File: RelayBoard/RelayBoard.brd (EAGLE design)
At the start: 139.1 x 115.2 mm, 97 parts, among them IC1 MCP2551/SN RSC 402-904, J4 JTAG_ARM_10PIN, U1 CD74HC4067SM96, U2 LM1084IS-3.3, U3 CD74HC4067SM96, U4 CD74HC4067SM96, U5 CD74HC4067SM96, U6 LM1084IS-3.3, U7 LM1084IS-3.3, U8 TM4C1294NCPDT, X1 A1944-50, X2 A1944-50, X3 A1944-50, X4 A1944-50, Y3 NX3225GA, Y4 CRYATL_32K_SMD

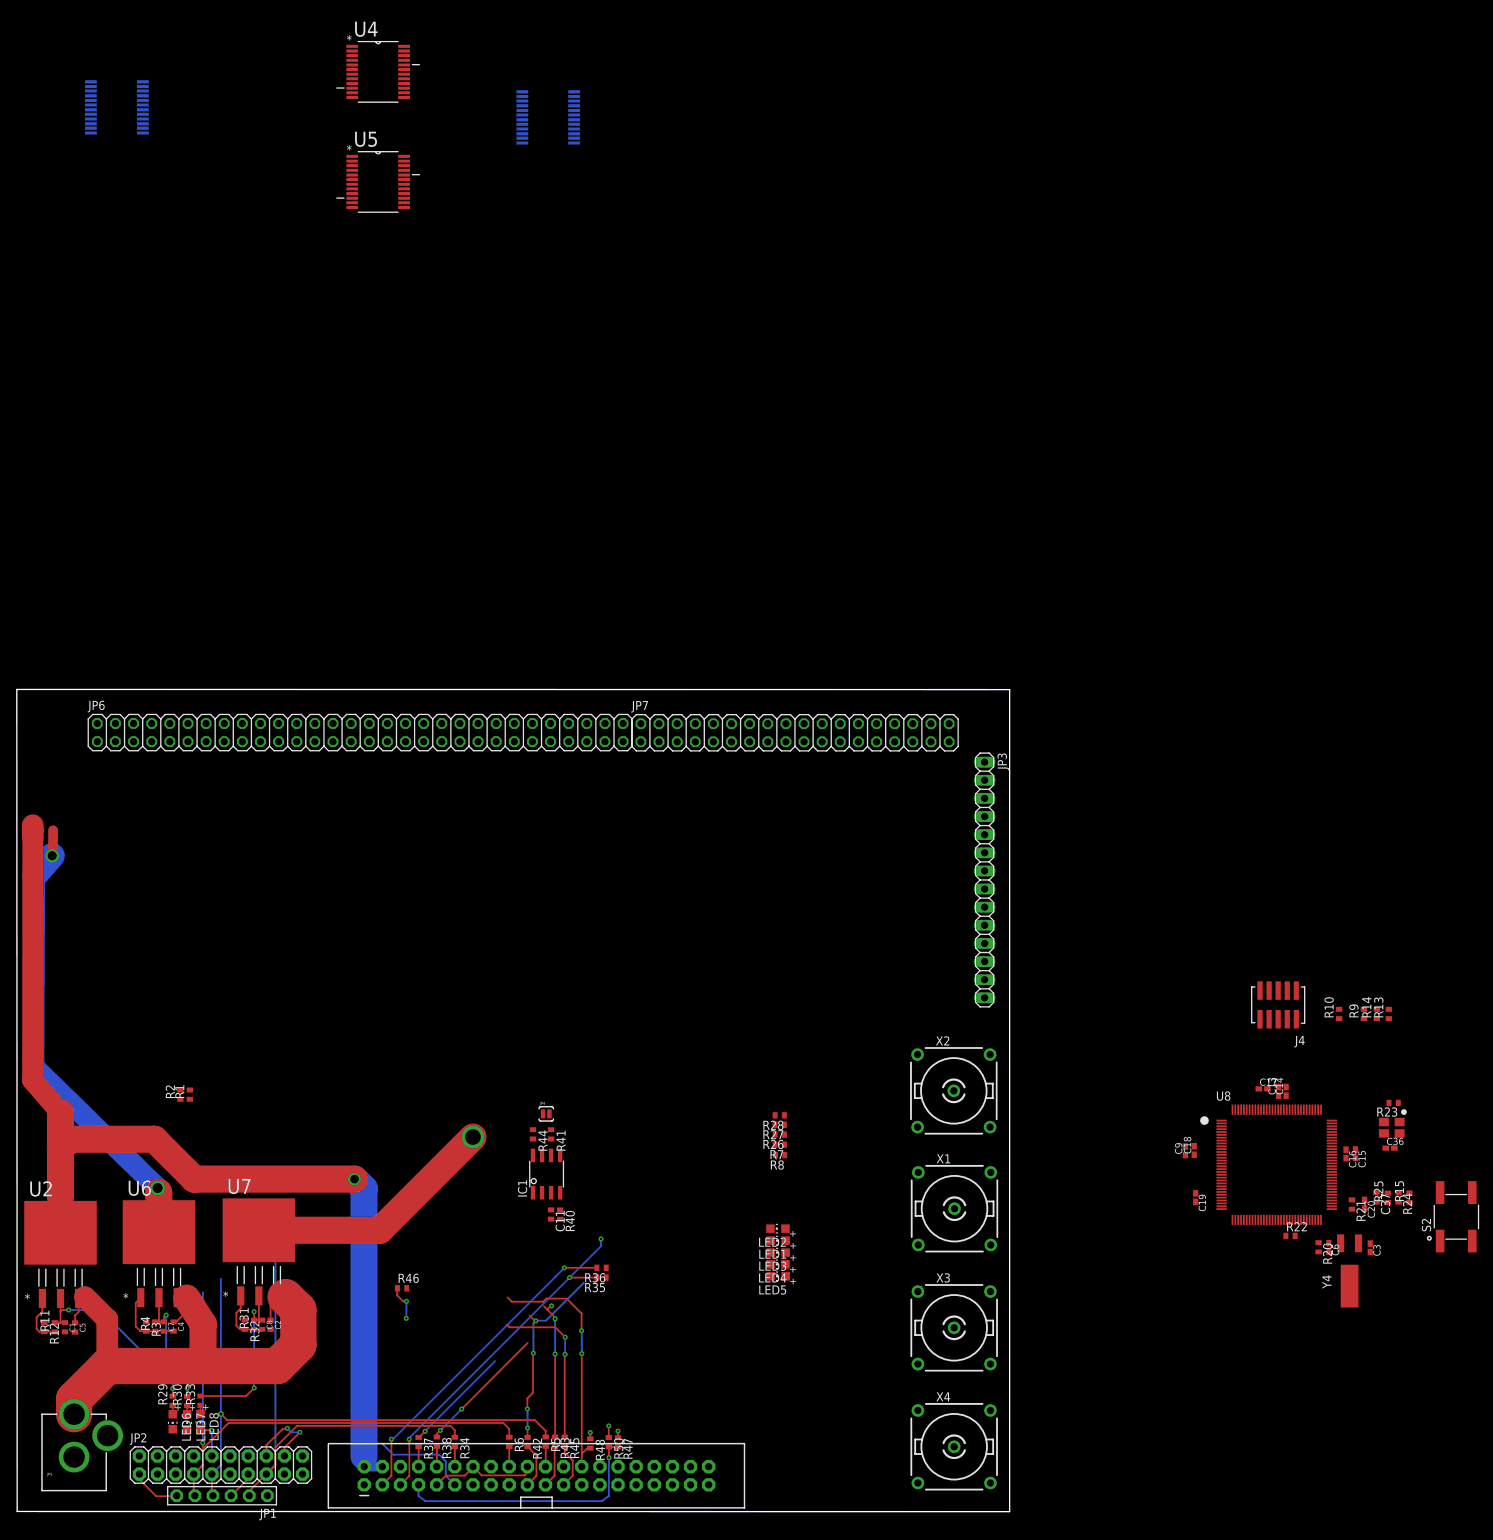
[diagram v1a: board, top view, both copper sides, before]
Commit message: additions
- common connector for isp, jtag, swd
- change LDOs to the one which have Enable pin
- UART -> USB interface and isolator to the uart side
- dedicated MCU supply
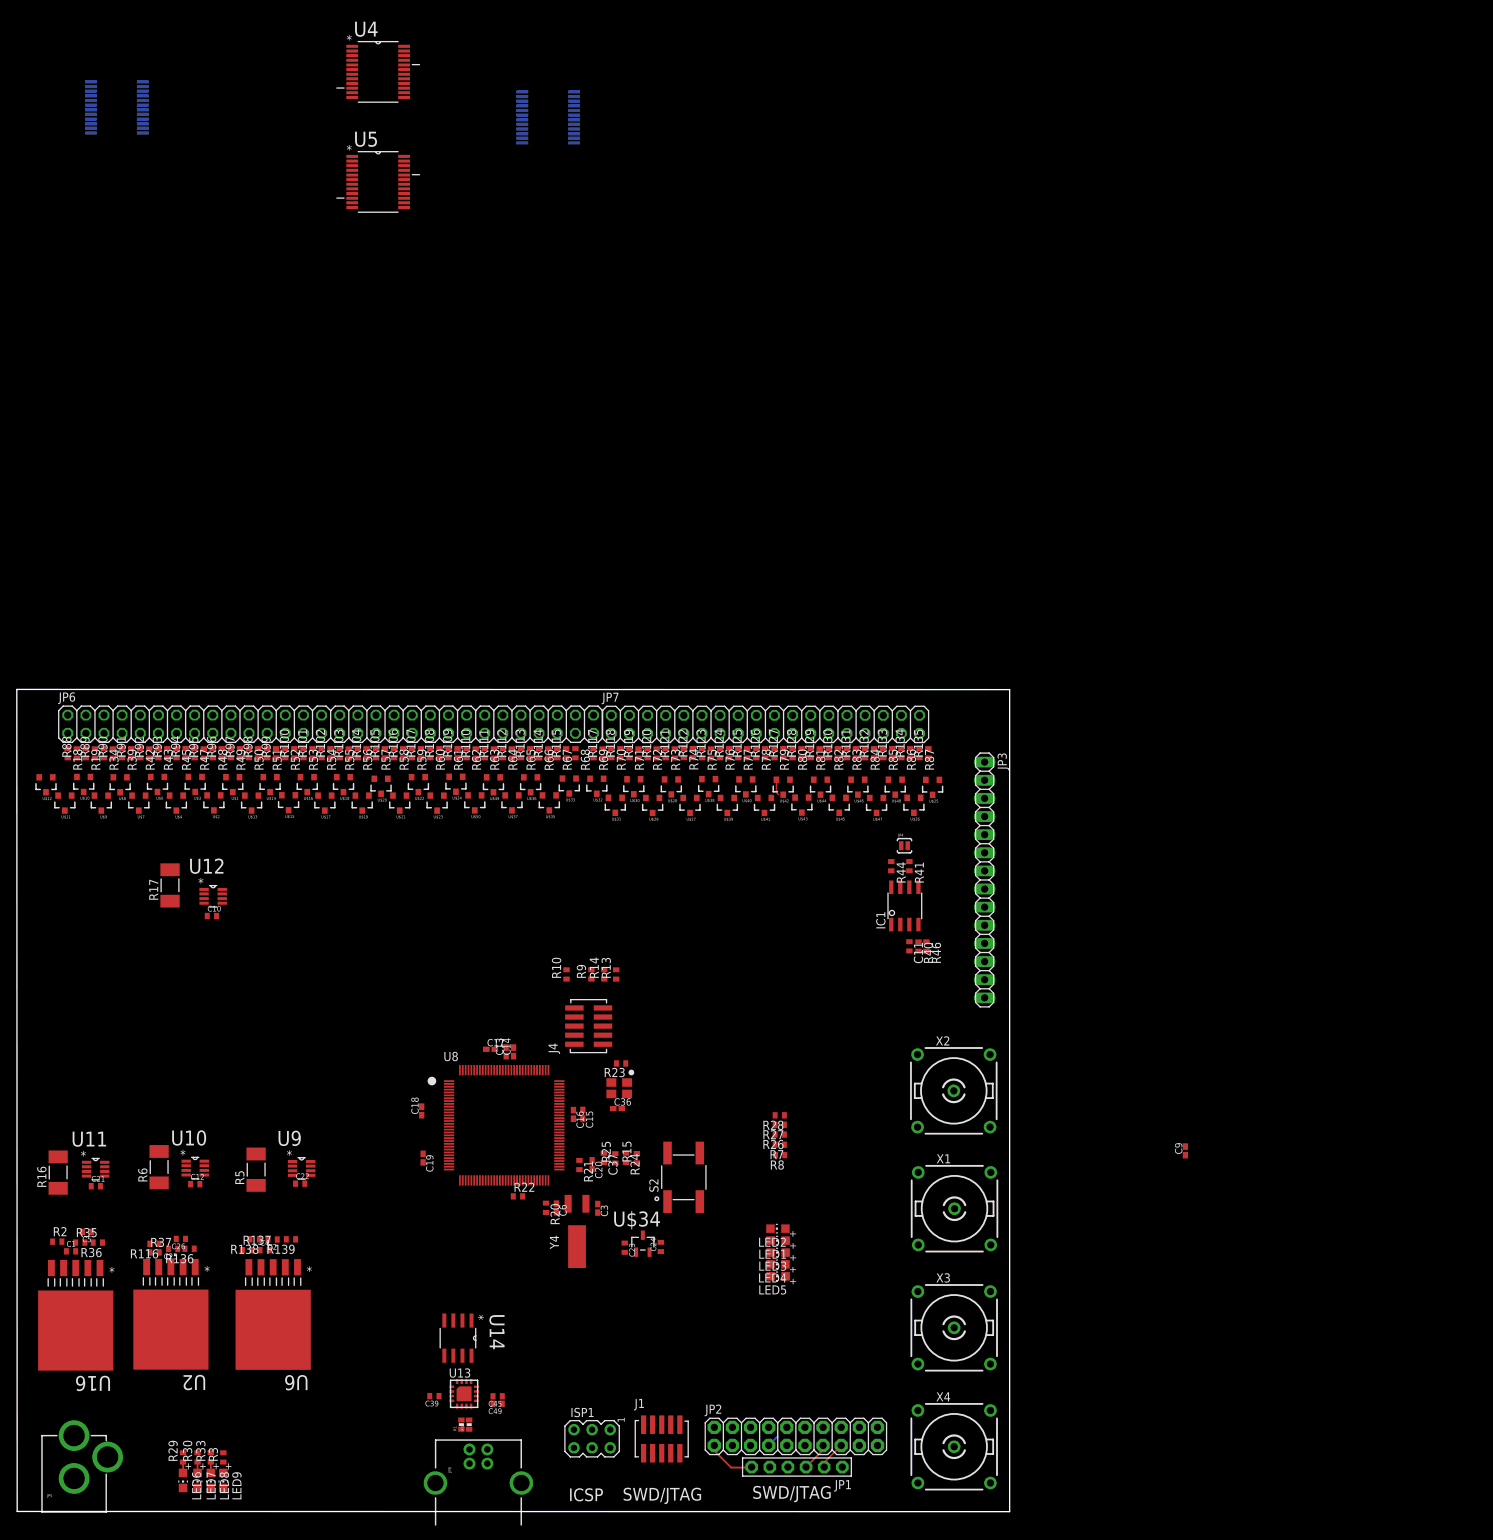
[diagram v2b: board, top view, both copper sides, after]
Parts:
- removed C7, C8: 10uF, rcl:C0402
- removed JP30: RASPBERRYPI-B+-GPIO, SparkFun-Boards:2X20-SHROUDED
- removed R11, R12, R31, R32, R4: (no value), resistor:R0402@1
- removed U7: LM1084IS-3.3, LDO:TO254P1435X457-3N
- added C10, C12, C21, C22, C39, C45: 0.1uF, rcl:C0402
- added C23, C24: 1uF, rcl:C0402
- added C25, C26, C49: 10uF, rcl:C0402
- added ISP1: AVRISP-6, JDT-1800_smahed:AVRISP
- added J1: JTAG_ARM_10PIN, MRDT-Connectors:CON_2X5_50MIL
- added JP8: USB-B, SparkFun-Connectors:USB-B-PTH
- added LED9: (no value), JDT-1800_smahed:CHIP-LED0805
- added R100, R101, R102, R103, R104, R105, R106, R107, R108, R109, R110, R111, R112, R113, R114, R115, R117, R118, R119, R120, R121, R122, R123, R124, R125, R126, R127, R128, R129, R130, R131, R132, R133, R134, R135, R18, R19, R39, R49, R51, R52, R53, R54, R55, R56, R57, R58, R59, R60, R61, R62, R63, R64, R65, R66, R67, R68, R69, R70, R71, R72, R73, R74, R75, R76, R77, R78, R79, R80, R81, R82, R83, R84, R85, R86, R87, R88, R89, R90, R91, R92, R93, R94, R95, R96, R97, R98, R99: 200R, resistor:R0402
- added R116, R136, R137, R138, R139: (no value), resistor:R0402
- added R16, R17: (no value), JDT-1800_smahed:R5025
- added U$1, U$10, U$11, U$12, U$13, U$14, U$15, U$16, U$17, U$18, U$19, U$2, U$20, U$21, U$22, U$23, U$24, U$25, U$26, U$27, U$28, U$29, U$3, U$30, U$31, U$32, U$33, U$35, U$36, U$37, U$38, U$39, U$4, U$40, U$41, U$42, U$43, U$44, U$45, U$46, U$47, U$48, U$49, U$50, U$6, U$7, U$8, U$9: zener_3.3V, SparkFun-DiscreteSemi:SOT23-3
- added U$34: MCP1703T-3302E/CB, MCP1703:SOT95P300X145-3N
- added U10, U11, U12, U9: INA219AIDCNR, INA219:SOT65P280X145-8N
- added U13: FT230XQ, ftdichip:QFN16
- added U14: ADUM1201ARZ, ADUM1201ARZ:SOIC127P600X175-8N
- added U16: TL1963AKTTR., TL1963:TO170P1485X457-6N
- C2, C4, C5: value 0.1uF -> 10uF
- R1, R38: value (none) -> 22R; device resistor:R0402@1 -> SparkFun-Passives:0402-RES
- R10, R13, R14, R15, R2, R26, R27, R28, R29, R3, R30, R33, R35, R36, R37, R40, R41, R44, R46, R7, R8, R9: device resistor:R0402@1 -> resistor:R0402
- R34, R42, R43, R45, R50: value 0R -> 200R; device resistor:R0402@1 -> resistor:R0402
- R47, R48: value 10k -> 200R; device resistor:R0402@1 -> resistor:R0402
- R5, R6: value 0R -> (none); device resistor:R0402@1 -> JDT-1800_smahed:R5025
- U2, U6: value LM1084IS-3.3 -> TL1963AKTTR.; device LDO:TO254P1435X457-3N -> TL1963:TO170P1485X457-6N
- moved R47 113.3 mm to (25.2, 106.1)
- moved R43 111.3 mm to (20.1, 106.1)
- moved R45 110.7 mm to (22.7, 106.1)
- moved R42 110.7 mm to (17.6, 106.1)
- moved R48 110.2 mm to (27.8, 106.1)
- moved R50 108.9 mm to (32.8, 106.1)
- moved C16 108.4 mm to (78.3, 55.5)
- moved C17 108.4 mm to (66.7, 64.6)
- moved C36 108.4 mm to (84.5, 56.3)
- moved C37 108.4 mm to (82.5, 49.4)
- moved R21 108.4 mm to (79.1, 48.4)
- moved R25 108.4 mm to (84.2, 49.4)
- moved R9 108.4 mm to (80.8, 75.1)
- moved C13 108.4 mm to (68.9, 64.3)
- moved C14 108.4 mm to (69.9, 64.3)
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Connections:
- removed net +3V3: C16.1, C17.1, C18.1, C19.1, J4.P1, R20.2, R21.2, R25.1, U8.P$101, U8.P$113, U8.P$122, U8.P$16, U8.P$26, U8.P$28, U8.P$39, U8.P$47, U8.P$51, U8.P$52, U8.P$69, U8.P$7, U8.P$79, U8.P$8, U8.P$9, U8.P$90
- removed net 3.3V: JP30.17
- removed net 3.6V: C8.1, R31.2, R33.2, U7.2, U7.4
- removed net 5V: C1.1, JP30.2, JP30.4, R11.2, R29.2, U2.2, U2.4
- removed net A0: U3.17, U5.17
- removed net A1: U3.16, U5.16
- removed net A2: U3.19, U5.19
- removed net A3: U3.18, U5.18
- removed net ADJ: R3.2, R4.1, U6.1
- removed net ADJ1: R11.1, R12.2, U2.1
- removed net ADJ2: R31.1, R32.2, U7.1
- removed net CAN_CS: JP30.26, R48.2
- removed net D0: U3.21, U5.21
- removed net D1: U3.20, U5.20
- removed net D10: U3.9, U5.9
- removed net D11: U3.8, U5.8
- removed net D12: U1.17, U4.17
- removed net D13: U1.16, U4.16
- removed net D14: U1.19, U4.19
- removed net D15: U1.18, U4.18
- removed net D16: U1.21, U4.21
- removed net D17: U1.20, U4.20
- removed net D18: U1.23, U4.23
- removed net D19: U1.22, U4.22
- removed net D2: U3.23, U5.23
- removed net D20: U1.8, U4.8
- removed net D21: U1.9, U4.9
- removed net D22: U1.6, U4.6
- removed net D23: U1.7, U4.7
- removed net D24: U1.4, U4.4
- removed net D25: U1.5, U4.5
- removed net D26: U1.2, U4.2
- removed net D27: U1.3, U4.3
- removed net D3: U3.22, U5.22
- removed net D4: U3.4, U5.4
- removed net D5: U3.5, U5.5
- removed net D6: U3.2, U5.2
- removed net D7: U3.3, U5.3
- removed net D8: U3.7, U5.7
- removed net D9: U3.6, U5.6
- removed net IO_INT: JP30.11
- removed net NC0: JP30.1
- removed net RPI_NRESET: JP30.12, R34.2
- removed net RPI_SWDCLK: JP30.22, R5.2
- removed net RPI_SWDIO: JP30.18, R6.2
- removed net RX: J4.P7, JP3.10, R38.1, U8.P$33
- removed net SCK: R45.1
- removed net TARGET_CS: JP30.7, R47.2, R50.2
- removed net TFT_CS: JP30.24
- removed net TFT_MISO: JP30.21, R43.2
- removed net TFT_MOSI: JP30.19, R42.2
- removed net TFT_RX: JP30.8, R37.2
- removed net TFT_SCK: JP30.23, R45.2
- removed net TFT_SCL: JP30.5, R1.1, R35.2
- removed net TFT_SDA: JP30.3, R2.1, R36.2
- removed net TFT_TX: JP30.10, R38.2
- removed net TX: J4.P9, JP3.11, R37.1, U8.P$34
- removed net VOLTAGE_INPUT: C2.1, C4.1, C5.1, JP5.PWR, U2.3, U6.3, U7.3
- new net ADJ3: R2.1, R35.2, U16.5
- new net ADJ4: R116.2, R37.1, U2.5
- new net ADJ5: R137.1, R138.2, U6.5
- new net DUT_SH+: R17.2, U12.1
- new net DUT_SH_-: R17.1, U12.2
- new net HOST_GND: C39.1, C45.1, C49.1, U13.13, U13.3, U14.5
- new net HOST_UART_RX: U13.2, U14.6
- new net HOST_UART_TX: U13.15, U14.2
- new net LDO1: R108.1, R16.2, R29.2, R60.2, U$22.1, U$22.2, U11.2
- new net LDO1_ENABLE: R36.1, U16.1
- new net LDO1_SH+: C1.1, R16.1, R2.2, U11.1, U16.4
- new net LDO2: R109.1, R30.2, R6.2, R61.2, U$23.1, U$23.2, U10.2
- new net LDO2_ENABLE: R136.1, U2.1
- new net LDO2_SH+: C2.1, R37.2, R6.1, U10.1, U2.4
- new net LDO3: R110.1, R33.2, R5.2, R62.2, U$24.1, U$24.2, U9.2
- new net LDO3_ENABLE: R139.1, U6.1
- new net LDO3_SH+: C4.1, R137.2, R5.1, U6.4, U9.1
- new net M0S0: U4.10
- new net M0S1: U4.11
- new net M0S2: U4.14
- new net M0S3: U4.13
- new net M3S0: U5.10
- new net M3S1: U5.11
- new net M3S2: U5.14
- new net M3S3: U5.13
- new net N$10: JP6.11, R43.1
- new net N$100: JP6.38, R106.2
- new net N$101: JP6.40, R107.2
- new net N$102: JP6.42, R108.2
- new net N$103: JP6.44, R109.2
- new net N$104: JP6.46, R110.2
- new net N$105: JP6.48, R111.2
- new net N$106: JP6.50, R112.2
- new net N$107: JP6.52, R113.2
- new net N$108: JP6.54, R114.2
- new net N$109: JP6.56, R115.2
- new net N$11: JP6.13, R45.1
- new net N$110: LED9.A, R3.1
- new net N$111: JP6.60, R117.2
- new net N$112: R18.2, U$12.2
- new net N$113: R87.2, U$25.2
- new net N$114: R88.1, U$12.1
- new net N$115: R89.1, U$11.1
- new net N$116: R19.2, U$11.2
- new net N$117: R90.1, U$10.1
- new net N$118: R34.2, U$10.2
- new net N$119: R91.1, U$9.1
- new net N$12: JP6.15, R47.1
- new net N$120: R39.2, U$9.2
- new net N$121: R92.1, U$8.1
- new net N$122: R42.2, U$8.2
- new net N$123: R43.2, U$7.2
- new net N$124: R93.1, U$7.1
- new net N$125: R94.1, U$6.1
- new net N$126: R45.2, U$6.2
- new net N$127: R47.2, U$4.2
- new net N$128: R95.1, U$4.1
- new net N$129: R96.1, U$3.1
- new net N$13: JP6.17, R48.1
- new net N$130: R48.2, U$3.2
- new net N$131: R97.1, U$2.1
- new net N$132: R49.2, U$2.2
- new net N$133: R50.2, U$1.2
- new net N$134: R98.1, U$1.1
- new net N$135: R99.1, U$13.1
- new net N$136: R51.2, U$13.2
- new net N$137: R52.2, U$14.2
- new net N$138: R100.1, U$14.1
- new net N$139: R101.1, U$15.1
- new net N$14: JP6.19, R49.1
- new net N$140: R53.2, U$15.2
- new net N$141: R54.2, U$16.2
- new net N$142: R102.1, U$16.1
- new net N$143: R55.2, U$17.2
- new net N$144: R103.1, U$17.1
- new net N$145: R104.1, U$18.1
- new net N$146: R56.2, U$18.2
- new net N$147: R105.1, U$19.1
- new net N$148: R57.2, U$19.2
- new net N$149: R106.1, U$20.1
- new net N$15: JP6.21, R50.1
- new net N$150: R58.2, U$20.2
- new net N$151: R59.2, U$21.2
- new net N$152: R107.1, U$21.1
- new net N$157: R135.1, U$25.1
- new net N$159: C39.2, U13.8
- new net N$16: JP6.23, R51.1
- new net N$160: R134.1, U$26.1
- new net N$161: R86.2, U$26.2
- new net N$162: R85.2, U$48.2
- new net N$163: R133.1, U$48.1
- new net N$164: R84.2, U$47.2
- new net N$165: R83.2, U$46.2
- new net N$166: R82.2, U$45.2
- new net N$167: R81.2, U$44.2
- new net N$168: R80.2, U$43.2
- new net N$169: R79.2, U$42.2
- new net N$17: JP6.25, R52.1
- new net N$170: R78.2, U$41.2
- new net N$171: R77.2, U$40.2
- new net N$172: R76.2, U$39.2
- new net N$173: R75.2, U$38.2
- new net N$174: R73.2, U$28.2
- new net N$175: R72.2, U$29.2
- new net N$176: R71.2, U$30.2
- new net N$177: R70.2, U$31.2
- new net N$178: R69.2, U$32.2
- new net N$179: R68.2, U$33.1
- new net N$18: JP6.27, R53.1
- new net N$180: R67.2, U$35.2
- new net N$181: R66.2, U$36.2
- new net N$182: R129.1, U$44.1
- new net N$183: R132.1, U$47.1
- new net N$184: R131.1, U$46.1
- new net N$185: R130.1, U$45.1
- new net N$186: R74.2, U$27.2
- new net N$187: R128.1, U$43.1
- new net N$188: R127.1, U$42.1
- new net N$189: R65.2, U$37.2
- new net N$19: JP6.29, R54.1
- new net N$190: R64.2, U$49.2
- new net N$191: R63.2, U$50.2
- new net N$192: R126.1, U$41.1
- new net N$193: R125.1, U$40.1
- new net N$194: R124.1, U$39.1
- new net N$195: R123.1, U$38.1
- new net N$196: R122.1, U$27.1
- new net N$197: R121.1, U$28.1
- new net N$198: R120.1, U$29.1
- new net N$199: R119.1, U$30.1
- new net N$20: JP6.31, R55.1
- new net N$200: R118.1, U$31.1
- new net N$201: R117.1, U$32.1
- new net N$203: R115.1, U$33.2
- new net N$204: R114.1, U$36.1
- new net N$205: R113.1, U$37.1
- new net N$206: R112.1, U$49.1
- new net N$207: R111.1, U$50.1
- new net N$21: JP6.33, R56.1
- new net N$216: C23.1, U$34.3
- new net N$22: JP6.35, R57.1
- new net N$24: JP6.37, R58.1
- new net N$26: JP6.39, R59.1
- new net N$27: JP6.41, R60.1
- new net N$28: JP6.43, R61.1
- new net N$29: JP6.45, R62.1
- new net N$30: JP6.47, R63.1
- new net N$31: JP6.49, R64.1
- new net N$32: JP6.51, R65.1
- new net N$37: JP6.53, R66.1
- new net N$38: JP6.55, R67.1
- new net N$39: JP6.57, R68.1
- new net N$4: JP6.1, R18.1
- new net N$40: JP6.59, R69.1
- new net N$41: JP7.1, R70.1
- new net N$42: JP7.3, R71.1
- new net N$43: JP7.5, R72.1
- new net N$49: JP7.7, R73.1
- new net N$50: JP7.9, R74.1
- new net N$51: JP7.11, R75.1
- new net N$52: JP7.13, R76.1
- new net N$53: JP7.15, R77.1
- new net N$54: JP7.17, R78.1
- new net N$55: JP7.19, R79.1
- new net N$56: JP7.21, R80.1
- new net N$57: JP7.23, R81.1
- new net N$58: JP7.25, R82.1
- new net N$59: JP7.27, R83.1
- new net N$6: JP6.3, R19.1
- new net N$60: JP7.29, R84.1
- new net N$61: JP7.31, R85.1
- new net N$62: JP7.33, R86.1
- new net N$63: JP7.35, R87.1
- new net N$64: JP7.2, R118.2
- new net N$65: JP7.4, R119.2
- new net N$66: JP7.6, R120.2
- new net N$67: JP7.8, R121.2
- new net N$68: JP7.10, R122.2
- new net N$69: JP7.12, R123.2
- new net N$7: JP6.5, R34.1
- new net N$70: JP7.14, R124.2
- new net N$71: JP7.16, R125.2
- new net N$72: JP7.18, R126.2
- new net N$73: JP7.20, R127.2
- new net N$74: JP7.22, R128.2
- new net N$75: JP7.24, R129.2
- new net N$76: JP7.26, R130.2
- new net N$77: JP7.28, R131.2
- new net N$78: JP7.30, R132.2
- new net N$79: JP7.32, R133.2
- new net N$8: JP6.7, R39.1
- new net N$80: JP7.34, R134.2
- new net N$81: JP7.36, R135.2
- new net N$82: JP6.2, R88.2
- new net N$83: JP6.4, R89.2
- new net N$84: JP6.6, R90.2
- new net N$85: JP6.8, R91.2
- new net N$86: JP6.10, R92.2
- new net N$87: JP6.12, R93.2
- new net N$88: JP6.14, R94.2
- new net N$89: JP6.16, R95.2
- new net N$9: JP6.9, R42.1
- new net N$90: JP6.18, R96.2
- new net N$91: JP6.20, R97.2
- new net N$92: JP6.22, R98.2
- new net N$93: JP6.24, R99.2
- new net N$94: JP6.26, R100.2
- new net N$95: JP6.28, R101.2
- new net N$96: JP6.30, R102.2
- new net N$97: JP6.32, R103.2
- new net N$98: JP6.34, R104.2
- new net N$99: JP6.36, R105.2
- new net POWER_IN: C25.1, C26.1, C5.1, JP5.PWR, U16.2, U2.2, U6.2
- new net SWDCLK/TCLK/SCK: ISP1.3, J1.P4, JP2.9
- new net SWDIO/TMS: J1.P2, JP2.7
- new net SWO/TDO/MISO: ISP1.1, J1.P6, JP2.13
- new net TDI/MISO: JP2.5
- new net TDI/MOSI: ISP1.4, J1.P8
- new net TRST_3V3: R136.2, R139.2, R36.2
- new net TSTR_3V3: C10.1, C12.1, C16.1, C17.1, C18.1, C19.1, C21.1, C22.2, C24.1, ISP1.2, J1.P1, J4.P1, R20.2, R21.2, R25.1, R3.2, U$34.2, U10.4, U10.8, U11.4, U11.7, U12.4, U14.1, U8.P$101, U8.P$113, U8.P$122, U8.P$16, U8.P$26, U8.P$28, U8.P$39, U8.P$47, U8.P$51, U8.P$52, U8.P$69, U8.P$7, U8.P$79, U8.P$8, U8.P$9, U8.P$90, U9.4, U9.7, U9.8
- new net TSTR_RX: J4.P7, JP3.10, U14.7, U8.P$33
- new net TSTR_SCL: U10.5, U11.5, U12.5, U9.5
- new net TSTR_SDA: U10.6, U11.6, U12.6, U9.6
- new net TSTR_TX: J4.P9, JP3.11, U14.3, U8.P$34
- new net USBD_N: R38.2, U13.7
- new net USBD_P: R1.2, U13.6
- new net USB_N: JP8.D-, R38.1
- new net USB_P: JP8.D+, R1.1
- new net VBUS: C45.2, C49.2, JP8.VBUS, U13.1, U13.10, U14.8
- net CS: no longer R50.1
- net GND: now also C10.2, C12.2, C21.2, C22.1, C23.2, C24.2, C25.2, C26.2, ISP1.6, J1.P5, LED9.C, R116.1, R138.1, R35.1, U$1.3, U$10.3, U$11.3, U$12.3, U$13.3, U$14.3, U$15.3, U$16.3, U$17.3, U$18.3, U$19.3, U$2.3, U$20.3, U$21.3, U$22.3, U$23.3, U$24.3, U$25.3, U$26.3, U$27.3, U$28.3, U$29.3, U$3.3, U$30.3, U$31.3, U$32.3, U$33.3, U$34.1, U$35.3, U$36.3, U$37.3, U$38.3, U$39.3, U$4.3, U$40.3, U$41.3, U$42.3, U$43.3, U$44.3, U$45.3, U$46.3, U$47.3, U$48.3, U$49.3, U$50.3, U$6.3, U$7.3, U$8.3, U$9.3, U10.3, U10.7, U11.3, U11.8, U12.3, U12.7, U12.8, U14.4, U16.3, U16.6, U2.3, U2.6, U6.3, U6.6, U9.3; no longer C7.2, C8.2, JP30.14, JP30.20, JP30.25, JP30.30, JP30.34, JP30.39, JP30.6, JP30.9, R12.1, R3.1, R32.1
- net M1S0: no longer U4.10
- net M1S1: no longer U4.11
- net M1S2: no longer U4.14
- net M1S3: no longer U4.13
- net M2S0: no longer U5.10
- net M2S1: no longer U5.11
- net M2S2: no longer U5.14
- net M2S3: no longer U5.13
- net MISO: no longer R43.1
- net MOSI: no longer R42.1
- net NRESET: now also ISP1.5, J1.P10; no longer R34.1
- net SCL: no longer R35.1
- net SDA: no longer R36.1
- net SWDCLK: no longer JP2.9, R5.1
- net SWDIO: no longer JP2.7, R6.1
- net SWO: no longer JP2.13
- net VCC: no longer C7.1, R1.2, R2.2, R30.2, R4.2, R47.1, R48.1, U6.2, U6.4
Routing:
- net 5V: track 177.1 -> 0.00 mm, vias 3 -> 0
- net VCC: track 93.9 -> 6.98 mm, vias 6 -> 0
- net VOLTAGE_INPUT: track 79.8 -> 0.00 mm
- net SWDCLK: track 78.3 -> 0.22 mm, vias 1 -> 0
- net SWDIO: track 76.8 -> 0.22 mm, vias 1 -> 0
- net NRESET: track 70.8 -> 4.01 mm
- net 3.6V: track 59.8 -> 0.00 mm, vias 3 -> 0
- net TFT_SCL: track 49.9 -> 0.00 mm, vias 3 -> 0
- net TFT_SDA: track 45.6 -> 0.00 mm, vias 2 -> 0
- net GND: track 38.6 -> 0.00 mm, vias 5 -> 0
- net TARGET_CS: track 36.9 -> 0.00 mm, vias 1 -> 0
- net CAN_CS: track 34.7 -> 0.00 mm, vias 2 -> 0
- net MOSI: track 27.0 -> 0.00 mm, vias 4 -> 0
- net SCK: track 22.9 -> 0.00 mm, vias 2 -> 0
- net MISO: track 19.8 -> 0.00 mm, vias 3 -> 0
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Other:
- board text added: "ICSP"
- board text added: "SWD/JTAG"
